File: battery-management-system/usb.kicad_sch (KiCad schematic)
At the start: 20 parts, among them J7 AMPHENOL_micro_usb_10118194-0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, U3 FT230XS

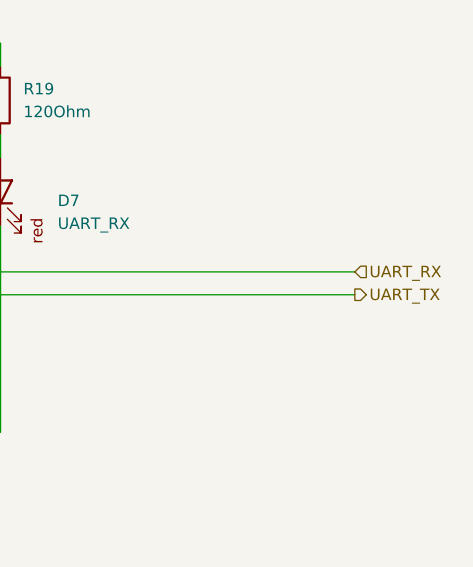
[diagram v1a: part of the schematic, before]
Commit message: add balancing sheet
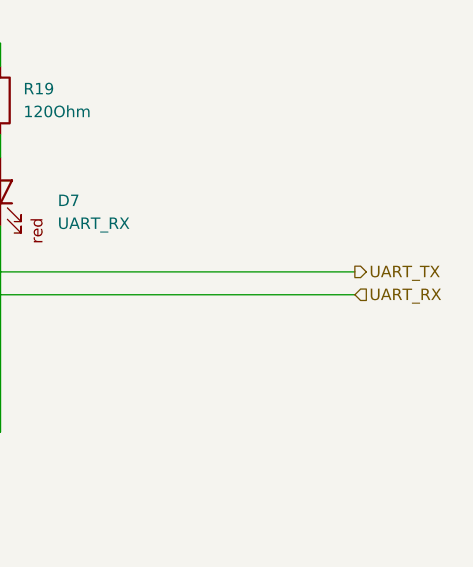
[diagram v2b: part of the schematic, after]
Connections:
- net UART_RX: now also R15.2, U3.4 (RXD); no longer R14.2, U3.1 (TXD)
- net UART_TX: now also R14.2, U3.1 (TXD); no longer R15.2, U3.4 (RXD)
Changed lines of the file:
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@@
     (stroke (width 0) (type default))
   )
-  (hierarchical_label "UART_TX" (shape output) (at 257.81 87.63 0) (fields_autoplaced)
+  (hierarchical_label "UART_RX" (shape input) (at 257.81 87.63 0) (fields_autoplaced)
     (effects (font (size 1.27 1.27)) (justify left))
   )
-  (hierarchical_label "UART_RX" (shape input) (at 257.81 85.09 0) (fields_autoplaced)
+  (hierarchical_label "UART_TX" (shape output) (at 257.81 85.09 0) (fields_autoplaced)
     (effects (font (size 1.27 1.27)) (justify left))
   )

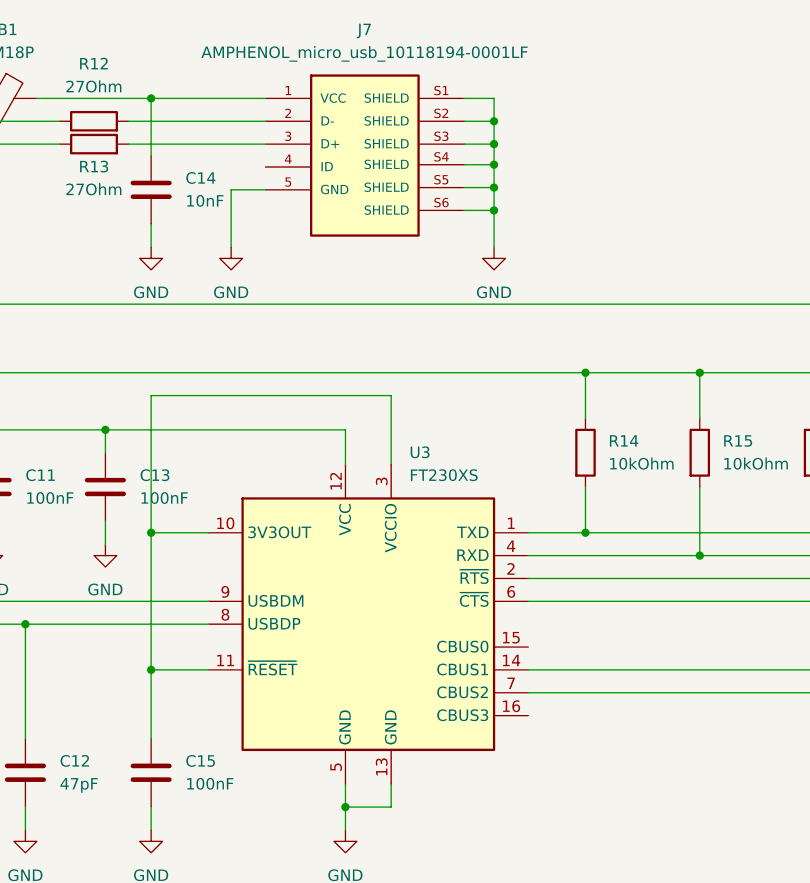
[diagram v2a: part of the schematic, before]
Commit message: fix electrical rule checker errors
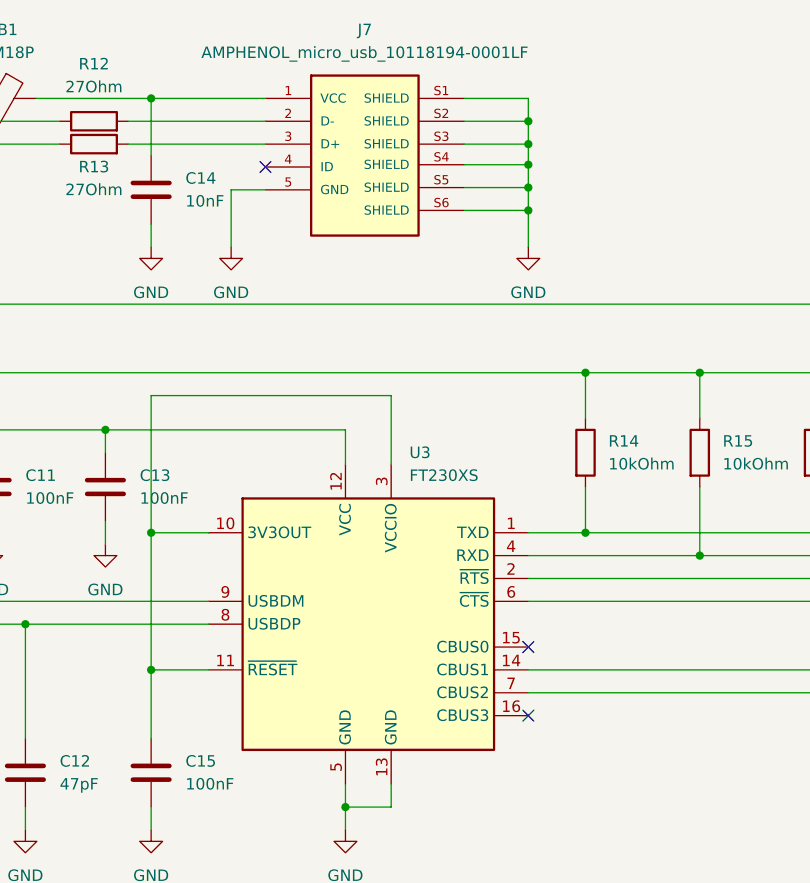
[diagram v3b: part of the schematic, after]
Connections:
- no-connect marks 0 -> 3
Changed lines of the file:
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@@
 (kicad_sch (version 20230121) (generator eeschema)
   (paper "A4")
-  (junction (at 139.7 46.736) (diameter 0) (color 0 0 0 0)
+  (junction (at 143.51 46.736) (diameter 0) (color 0 0 0 0)
   )
   (junction (at 162.56 67.31) (diameter 0) (color 0 0 0 0)
@@
   (junction (at 87.63 95.25) (diameter 0) (color 0 0 0 0)
   )
-  (junction (at 139.7 44.196) (diameter 0) (color 0 0 0 0)
-  )
-  (junction (at 139.7 49.276) (diameter 0) (color 0 0 0 0)
+  (junction (at 143.51 44.196) (diameter 0) (color 0 0 0 0)
+  )
+  (junction (at 143.51 49.276) (diameter 0) (color 0 0 0 0)
   )
   (junction (at 101.6 36.83) (diameter 0) (color 0 0 0 0)
@@
   (junction (at 149.86 67.31) (diameter 0) (color 0 0 0 0)
   )
-  (junction (at 139.7 39.37) (diameter 0) (color 0 0 0 0)
+  (junction (at 143.51 39.37) (diameter 0) (color 0 0 0 0)
   )
   (junction (at 96.52 73.66) (diameter 0) (color 0 0 0 0)
@@
   (junction (at 123.19 115.57) (diameter 0) (color 0 0 0 0)
   )
-  (junction (at 139.7 41.91) (diameter 0) (color 0 0 0 0)
+  (junction (at 143.51 41.91) (diameter 0) (color 0 0 0 0)
   )
   (junction (at 201.93 59.69) (diameter 0) (color 0 0 0 0)
   )
+  (no_connect (at 114.3 44.45))
+  (no_connect (at 143.51 105.41))
+  (no_connect (at 143.51 97.79))
   (wire (pts (xy 123.19 115.57) (xy 123.19 118.11))
     (stroke (width 0) (type default))
   )
-  (wire (pts (xy 139.7 39.37) (xy 139.7 41.91))
-    (stroke (width 0) (type default))
-  )
-  (wire (pts (xy 136.398 46.736) (xy 139.7 46.736))
-    (stroke (width 0) (type default))
-  )
-  (wire (pts (xy 136.398 44.196) (xy 139.7 44.196))
+  (wire (pts (xy 143.51 39.37) (xy 143.51 41.91))
+    (stroke (width 0) (type default))
+  )
+  (wire (pts (xy 136.398 46.736) (xy 143.51 46.736))
+    (stroke (width 0) (type default))
+  )
+  (wire (pts (xy 136.398 44.196) (xy 143.51 44.196))
     (stroke (width 0) (type default))
   )
@@
     (stroke (width 0) (type default))
   )
-  (wire (pts (xy 139.7 41.91) (xy 139.7 44.196))
+  (wire (pts (xy 143.51 41.91) (xy 143.51 44.196))
     (stroke (width 0) (type default))
   )
@@
     (stroke (width 0) (type default))
   )
-  (wire (pts (xy 139.7 36.83) (xy 139.7 39.37))
+  (wire (pts (xy 143.51 36.83) (xy 143.51 39.37))
     (stroke (width 0) (type default))
   )
@@
     (stroke (width 0) (type default))
   )
-  (wire (pts (xy 136.398 39.37) (xy 139.7 39.37))
+  (wire (pts (xy 136.398 39.37) (xy 143.51 39.37))
     (stroke (width 0) (type default))
   )
@@
     (stroke (width 0) (type default))
   )
-  (wire (pts (xy 139.7 49.276) (xy 139.7 53.34))
+  (wire (pts (xy 143.51 49.276) (xy 143.51 53.34))
     (stroke (width 0) (type default))
   )
@@
     (stroke (width 0) (type default))
   )
-  (wire (pts (xy 136.398 49.276) (xy 139.7 49.276))
+  (wire (pts (xy 136.398 49.276) (xy 143.51 49.276))
     (stroke (width 0) (type default))
   )
@@
     (stroke (width 0) (type default))
   )
-  (wire (pts (xy 136.398 41.91) (xy 139.7 41.91))
-    (stroke (width 0) (type default))
-  )
-  (wire (pts (xy 136.398 36.83) (xy 139.7 36.83))
+  (wire (pts (xy 136.398 41.91) (xy 143.51 41.91))
+    (stroke (width 0) (type default))
+  )
+  (wire (pts (xy 136.398 36.83) (xy 143.51 36.83))
     (stroke (width 0) (type default))
   )
@@
     (stroke (width 0) (type default))
   )
-  (wire (pts (xy 139.7 46.736) (xy 139.7 49.276))
-    (stroke (width 0) (type default))
-  )
-  (wire (pts (xy 139.7 44.196) (xy 139.7 46.736))
+  (wire (pts (xy 143.51 46.736) (xy 143.51 49.276))
+    (stroke (width 0) (type default))
+  )
+  (wire (pts (xy 143.51 44.196) (xy 143.51 46.736))
     (stroke (width 0) (type default))
   )
@@
     )
   )
-  (symbol (lib_id "power:GND") (at 139.7 53.34 0) (unit 1)
-    (in_bom yes) (on_board yes) (dnp no) (fields_autoplaced)
-    (property "Reference" "#PWR0124" (at 139.7 59.69 0)
-      (effects (font (size 1.27 1.27)) hide)
-    )
-    (property "Value" "GND" (at 139.7 58.42 0)
+  (symbol (lib_id "power:GND") (at 143.51 53.34 0) (unit 1)
+    (in_bom yes) (on_board yes) (dnp no) (fields_autoplaced)
+    (property "Reference" "#PWR0124" (at 143.51 59.69 0)
+      (effects (font (size 1.27 1.27)) hide)
+    )
+    (property "Value" "GND" (at 143.51 58.42 0)
       (effects (font (size 1.27 1.27)))
     )
-    (property "Footprint" "" (at 139.7 53.34 0)
-      (effects (font (size 1.27 1.27)) hide)
-    )
-    (property "Datasheet" "" (at 139.7 53.34 0)
-      (effects (font (size 1.27 1.27)) hide)
-    )
+    (property "Footprint" "" (at 143.51 53.34 0)
+      (effects (font (size 1.27 1.27)) hide)
+    )
+    (property "Datasheet" "" (at 143.51 53.34 0)
+      (effects (font (size 1.27 1.27)) hide)
+    )

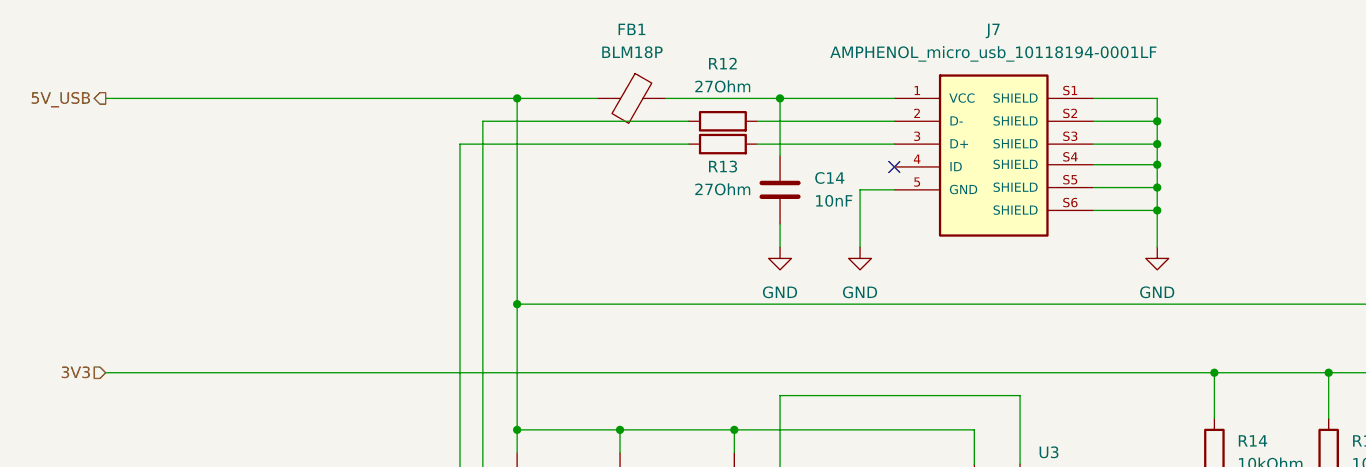
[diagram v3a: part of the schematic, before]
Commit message: fix current sensing
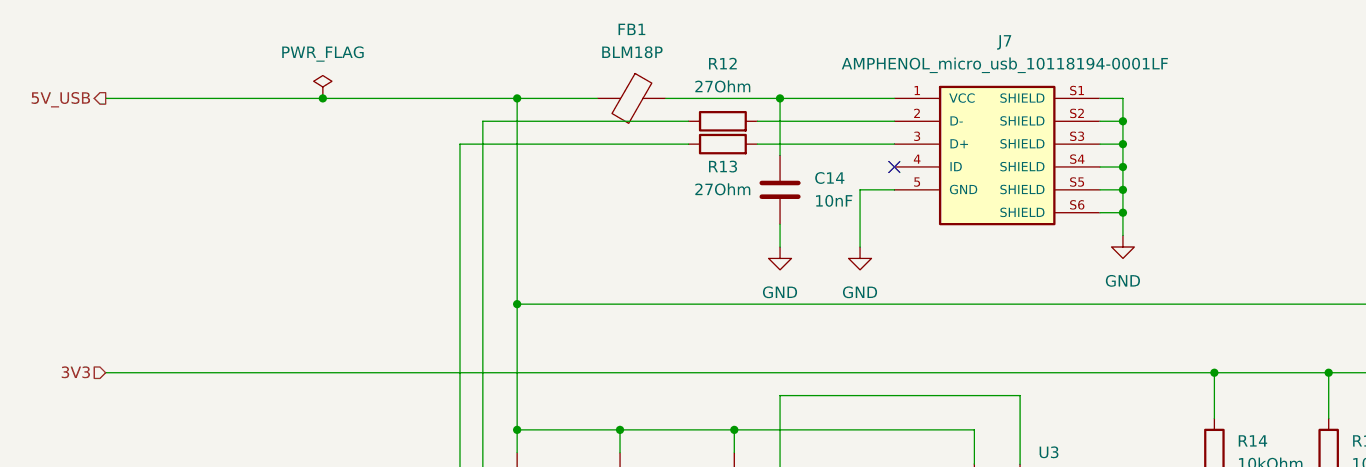
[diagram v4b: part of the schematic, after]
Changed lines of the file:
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@@
 (kicad_sch (version 20230121) (generator eeschema)
   (paper "A4")
-  (junction (at 143.51 46.736) (diameter 0) (color 0 0 0 0)
-  )
   (junction (at 162.56 67.31) (diameter 0) (color 0 0 0 0)
   )
+  (junction (at 139.7 46.99) (diameter 0) (color 0 0 0 0)
+  )
   (junction (at 101.6 85.09) (diameter 0) (color 0 0 0 0)
   )
+  (junction (at 139.7 44.45) (diameter 0) (color 0 0 0 0)
+  )
   (junction (at 87.63 95.25) (diameter 0) (color 0 0 0 0)
   )
-  (junction (at 143.51 44.196) (diameter 0) (color 0 0 0 0)
-  )
-  (junction (at 143.51 49.276) (diameter 0) (color 0 0 0 0)
+  (junction (at 50.8 36.83) (diameter 0) (color 0 0 0 0)
   )
   (junction (at 101.6 36.83) (diameter 0) (color 0 0 0 0)
@@
   (junction (at 101.6 100.33) (diameter 0) (color 0 0 0 0)
   )
+  (junction (at 139.7 39.37) (diameter 0) (color 0 0 0 0)
+  )
   (junction (at 72.39 73.66) (diameter 0) (color 0 0 0 0)
   )
@@
   (junction (at 162.56 87.63) (diameter 0) (color 0 0 0 0)
   )
+  (junction (at 139.7 41.91) (diameter 0) (color 0 0 0 0)
+  )
   (junction (at 72.39 59.69) (diameter 0) (color 0 0 0 0)
   )
   (junction (at 149.86 67.31) (diameter 0) (color 0 0 0 0)
   )
-  (junction (at 143.51 39.37) (diameter 0) (color 0 0 0 0)
-  )
   (junction (at 96.52 73.66) (diameter 0) (color 0 0 0 0)
   )
+  (junction (at 139.7 49.53) (diameter 0) (color 0 0 0 0)
+  )
   (junction (at 149.86 85.09) (diameter 0) (color 0 0 0 0)
   )
   (junction (at 123.19 115.57) (diameter 0) (color 0 0 0 0)
-  )
-  (junction (at 143.51 41.91) (diameter 0) (color 0 0 0 0)
   )
   (junction (at 201.93 59.69) (diameter 0) (color 0 0 0 0)
@@
     (stroke (width 0) (type default))
   )
-  (wire (pts (xy 143.51 39.37) (xy 143.51 41.91))
-    (stroke (width 0) (type default))
-  )
-  (wire (pts (xy 136.398 46.736) (xy 143.51 46.736))
-    (stroke (width 0) (type default))
-  )
-  (wire (pts (xy 136.398 44.196) (xy 143.51 44.196))
-    (stroke (width 0) (type default))
-  )
   (wire (pts (xy 101.6 85.09) (xy 107.95 85.09))
     (stroke (width 0) (type default))
@@
     (stroke (width 0) (type default))
   )
+  (wire (pts (xy 139.7 52.07) (xy 139.7 49.53))
+    (stroke (width 0) (type default))
+  )
   (wire (pts (xy 26.67 67.31) (xy 149.86 67.31))
     (stroke (width 0) (type default))
@@
     (stroke (width 0) (type default))
   )
+  (wire (pts (xy 139.7 41.91) (xy 139.7 39.37))
+    (stroke (width 0) (type default))
+  )
   (wire (pts (xy 201.93 59.69) (xy 218.44 59.69))
     (stroke (width 0) (type default))
@@
     (stroke (width 0) (type default))
   )
-  (wire (pts (xy 143.51 41.91) (xy 143.51 44.196))
-    (stroke (width 0) (type default))
-  )
   (wire (pts (xy 66.04 41.91) (xy 66.04 95.25))
     (stroke (width 0) (type default))
   )
+  (wire (pts (xy 137.16 49.53) (xy 139.7 49.53))
+    (stroke (width 0) (type default))
+  )
   (wire (pts (xy 123.19 115.57) (xy 128.27 115.57))
     (stroke (width 0) (type default))
@@
     (stroke (width 0) (type default))
   )
+  (wire (pts (xy 137.16 41.91) (xy 139.7 41.91))
+    (stroke (width 0) (type default))
+  )
   (wire (pts (xy 187.96 67.31) (xy 175.26 67.31))
     (stroke (width 0) (type default))
   )
+  (wire (pts (xy 50.8 36.83) (xy 72.39 36.83))
+    (stroke (width 0) (type default))
+  )
   (wire (pts (xy 128.27 69.85) (xy 101.6 69.85))
     (stroke (width 0) (type default))
@@
     (stroke (width 0) (type default))
   )
+  (wire (pts (xy 139.7 39.37) (xy 139.7 36.83))
+    (stroke (width 0) (type default))
+  )
   (wire (pts (xy 143.51 87.63) (xy 162.56 87.63))
     (stroke (width 0) (type default))
@@
     (stroke (width 0) (type default))
   )
-  (wire (pts (xy 143.51 36.83) (xy 143.51 39.37))
-    (stroke (width 0) (type default))
-  )
   (wire (pts (xy 72.39 73.66) (xy 83.82 73.66))
     (stroke (width 0) (type default))
@@
     (stroke (width 0) (type default))
   )
+  (wire (pts (xy 139.7 44.45) (xy 139.7 41.91))
+    (stroke (width 0) (type default))
+  )
   (wire (pts (xy 201.93 100.33) (xy 143.51 100.33))
     (stroke (width 0) (type default))
   )
+  (wire (pts (xy 137.16 44.45) (xy 139.7 44.45))
+    (stroke (width 0) (type default))
+  )
   (wire (pts (xy 162.56 67.31) (xy 175.26 67.31))
     (stroke (width 0) (type default))
@@
     (stroke (width 0) (type default))
   )
-  (wire (pts (xy 136.398 39.37) (xy 143.51 39.37))
-    (stroke (width 0) (type default))
-  )
   (wire (pts (xy 83.82 73.66) (xy 83.82 76.2))
     (stroke (width 0) (type default))
   )
-  (wire (pts (xy 143.51 49.276) (xy 143.51 53.34))
-    (stroke (width 0) (type default))
-  )
   (wire (pts (xy 72.39 36.83) (xy 81.28 36.83))
     (stroke (width 0) (type default))
   )
+  (wire (pts (xy 139.7 36.83) (xy 137.16 36.83))
+    (stroke (width 0) (type default))
+  )
   (wire (pts (xy 88.9 36.83) (xy 101.6 36.83))
     (stroke (width 0) (type default))
@@
     (stroke (width 0) (type default))
   )
-  (wire (pts (xy 136.398 49.276) (xy 143.51 49.276))
+  (wire (pts (xy 137.16 46.99) (xy 139.7 46.99))
     (stroke (width 0) (type default))
   )
@@
     (stroke (width 0) (type default))
   )
-  (wire (pts (xy 136.398 41.91) (xy 143.51 41.91))
-    (stroke (width 0) (type default))
-  )
-  (wire (pts (xy 136.398 36.83) (xy 143.51 36.83))
-    (stroke (width 0) (type default))
-  )
   (wire (pts (xy 128.27 113.03) (xy 128.27 115.57))
     (stroke (width 0) (type default))
@@
     (stroke (width 0) (type default))
   )
+  (wire (pts (xy 137.16 39.37) (xy 139.7 39.37))
+    (stroke (width 0) (type default))
+  )
   (wire (pts (xy 101.6 115.57) (xy 101.6 118.11))
     (stroke (width 0) (type default))
@@
     (stroke (width 0) (type default))
   )
-  (wire (pts (xy 26.67 36.83) (xy 72.39 36.83))
-    (stroke (width 0) (type default))
-  )
-  (wire (pts (xy 143.51 46.736) (xy 143.51 49.276))
-    (stroke (width 0) (type default))
-  )
-  (wire (pts (xy 143.51 44.196) (xy 143.51 46.736))
+  (wire (pts (xy 139.7 49.53) (xy 139.7 46.99))
+    (stroke (width 0) (type default))
+  )
+  (wire (pts (xy 26.67 36.83) (xy 50.8 36.83))
     (stroke (width 0) (type default))
   )
@@
   )
   (wire (pts (xy 83.82 73.66) (xy 96.52 73.66))
+    (stroke (width 0) (type default))
+  )
+  (wire (pts (xy 139.7 46.99) (xy 139.7 44.45))
     (stroke (width 0) (type default))
   )
@@
     )
   )
-  (symbol (lib_id "power:GND") (at 143.51 53.34 0) (unit 1)
-    (in_bom yes) (on_board yes) (dnp no) (fields_autoplaced)
-    (property "Reference" "#PWR0124" (at 143.51 59.69 0)
-      (effects (font (size 1.27 1.27)) hide)
-    )
-    (property "Value" "GND" (at 143.51 58.42 0)
-      (effects (font (size 1.27 1.27)))
-    )
-    (property "Footprint" "" (at 143.51 53.34 0)
-      (effects (font (size 1.27 1.27)) hide)
-    )
-    (property "Datasheet" "" (at 143.51 53.34 0)
+  (symbol (lib_id "power:GND") (at 139.7 52.07 0) (unit 1)
+    (in_bom yes) (on_board yes) (dnp no) (fields_autoplaced)
+    (property "Reference" "#PWR0124" (at 139.7 58.42 0)
+      (effects (font (size 1.27 1.27)) hide)
+    )
+    (property "Value" "GND" (at 139.7 57.15 0)
+      (effects (font (size 1.27 1.27)))
+    )
+    (property "Footprint" "" (at 139.7 52.07 0)
+      (effects (font (size 1.27 1.27)) hide)
+    )
+    (property "Datasheet" "" (at 139.7 52.07 0)
       (effects (font (size 1.27 1.27)) hide)
     )
@@
         (path "/5272f0ff-3069-41a9-bca2-80beede8b4b2/afdb149d-bd78-484c-a496-c5b66260efca"
           (reference "#PWR0119") (unit 1)
+        )
+      )
+    )
+  )
+  (symbol (lib_id "power:PWR_FLAG") (at 50.8 36.83 0) (unit 1)
+    (in_bom yes) (on_board yes) (dnp no) (fields_autoplaced)
+    (property "Reference" "#FLG05" (at 50.8 34.925 0)
+      (effects (font (size 1.27 1.27)) hide)
+    )
+    (property "Value" "PWR_FLAG" (at 50.8 31.75 0)
+      (effects (font (size 1.27 1.27)))
+    )
+    (property "Footprint" "" (at 50.8 36.83 0)
+      (effects (font (size 1.27 1.27)) hide)
+    )
+    (property "Datasheet" "~" (at 50.8 36.83 0)
+      (effects (font (size 1.27 1.27)) hide)
+    )
+    (pin "1")
+    (instances
+      (project "battery-management-system"
+        (path "/5272f0ff-3069-41a9-bca2-80beede8b4b2/afdb149d-bd78-484c-a496-c5b66260efca"
+          (reference "#FLG05") (unit 1)
         )
       )
@@
     )
   )
-  (symbol (lib_id "benediktibk:AMPHENOL_micro_usb_10118194-0001LF") (at 124.46 44.45 0) (unit 1)
-    (in_bom yes) (on_board yes) (dnp no) (fields_autoplaced)
-    (property "Reference" "J7" (at 125.349 29.21 0)
-      (effects (font (size 1.27 1.27)))
-    )
-    (property "Value" "AMPHENOL_micro_usb_10118194-0001LF" (at 125.349 31.75 0)
-      (effects (font (size 1.27 1.27)))
-    )
-    (property "Footprint" "benediktibk:AMPHENOL_10118194-0001LF" (at 125.6792 32.6136 0)
+  (symbol (lib_id "benediktibk:AMPHENOL_micro_usb_10118194-0001LF") (at 125.73 45.72 0) (unit 1)
+    (in_bom yes) (on_board yes) (dnp no) (fields_autoplaced)
+    (property "Reference" "J7" (at 126.619 30.48 0)
+      (effects (font (size 1.27 1.27)))
+    )
+    (property "Value" "AMPHENOL_micro_usb_10118194-0001LF" (at 126.619 33.02 0)
+      (effects (font (size 1.27 1.27)))
+    )
+    (property "Footprint" "benediktibk:AMPHENOL_10118194-0001LF" (at 126.9492 33.8836 0)
       (effects (font (size 1.27 1.27)) (justify bottom) hide)
     )
-    (property "Datasheet" "" (at 124.46 44.45 0)
-      (effects (font (size 1.27 1.27)) hide)
-    )
-    (property "RS order number" "137-0996" (at 124.46 44.45 0)
-      (effects (font (size 1.27 1.27)) hide)
-    )
+    (property "Datasheet" "" (at 125.73 45.72 0)
+      (effects (font (size 1.27 1.27)) hide)
+    )
+    (property "RS order number" "137-0996" (at 125.73 45.72 0)
+      (effects (font (size 1.27 1.27)) hide)
+    )

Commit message: improve layout
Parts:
- renumbered C9 to C15, C10 to C16, C11 to C17, C12 to C18, C13 to C19, C14 to C20, C15 to C21, D6 to D17, D7 to D18, J7 to J14, R12 to R19, R13 to R20, R14 to R21, R15 to R22, R16 to R23, R17 to R24, R18 to R25, R19 to R26, U3 to U6
